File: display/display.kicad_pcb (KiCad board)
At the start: 2 copper layers, 68.4 x 20.5 mm, 48 parts, among them P1 CONN_14

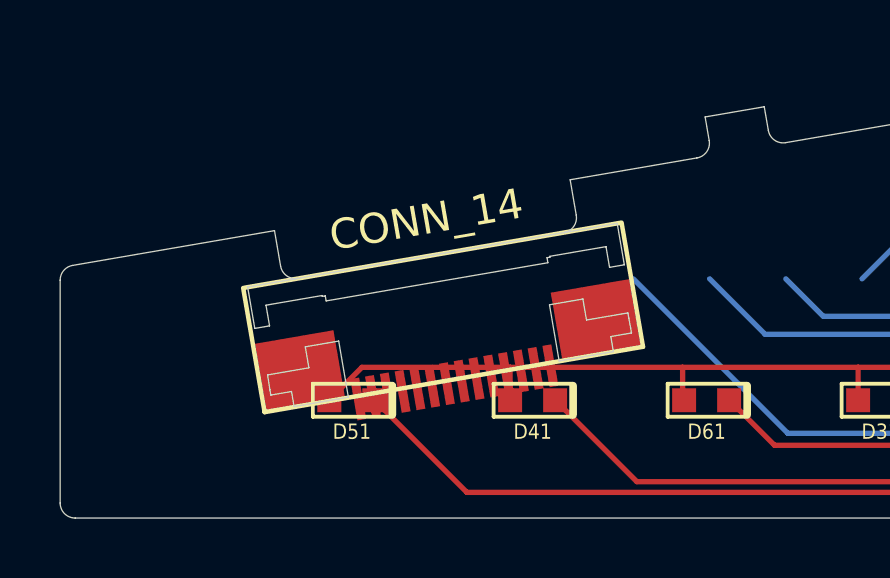
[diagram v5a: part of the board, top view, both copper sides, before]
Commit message: Remove the leftover contour lines of the connector.
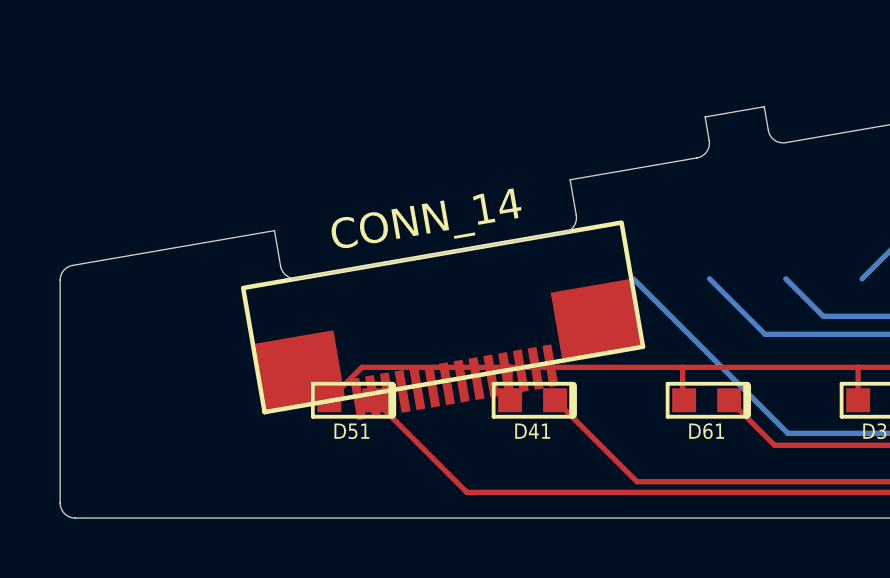
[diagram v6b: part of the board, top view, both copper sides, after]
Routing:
- net (no net): track 620.2 -> 699.0 mm, vias 29 -> 30
- net /COL7: track 78.8 -> 0.00 mm, vias 1 -> 0
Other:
- outline, holes or cut-outs redrawn

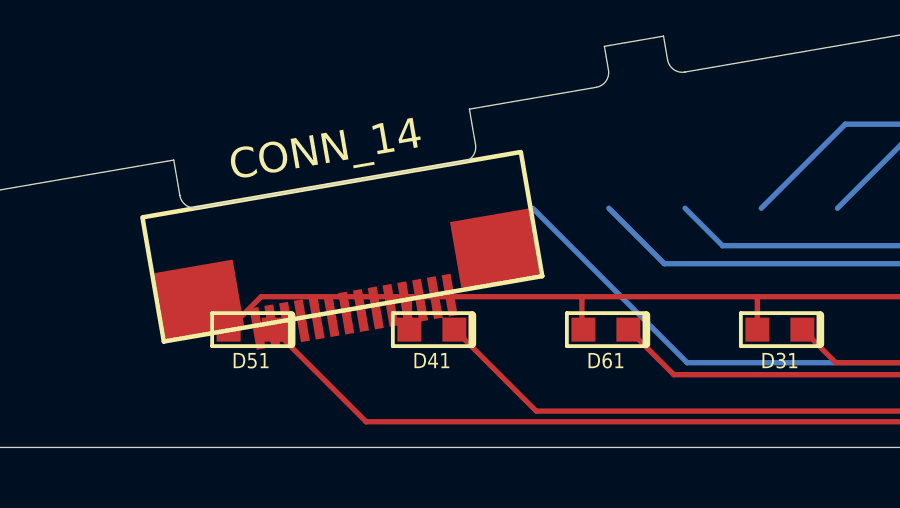
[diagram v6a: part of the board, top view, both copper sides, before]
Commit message: Remove D41 and D51 and the wires that were intersected the area of the connector.
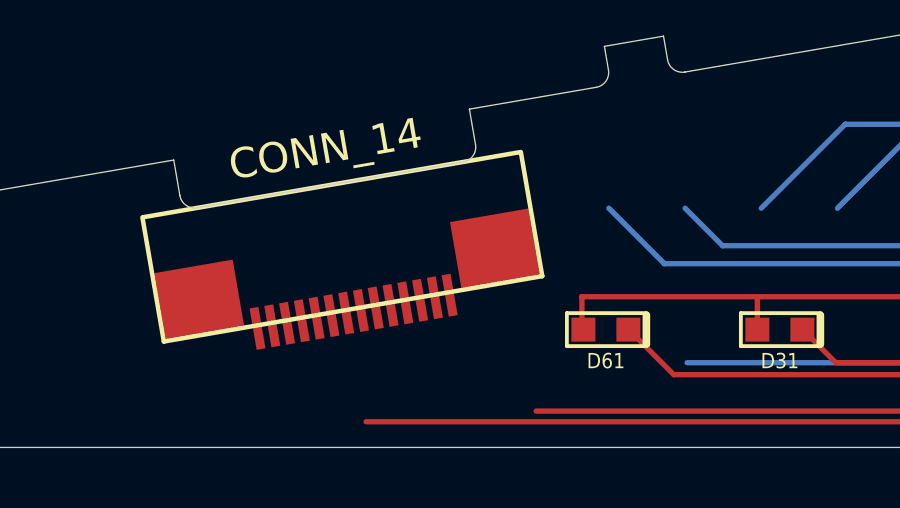
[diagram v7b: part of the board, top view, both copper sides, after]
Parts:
- removed D41, D51: LED, SM0603_Diode
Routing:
- net (no net): track 699.0 -> 670.2 mm

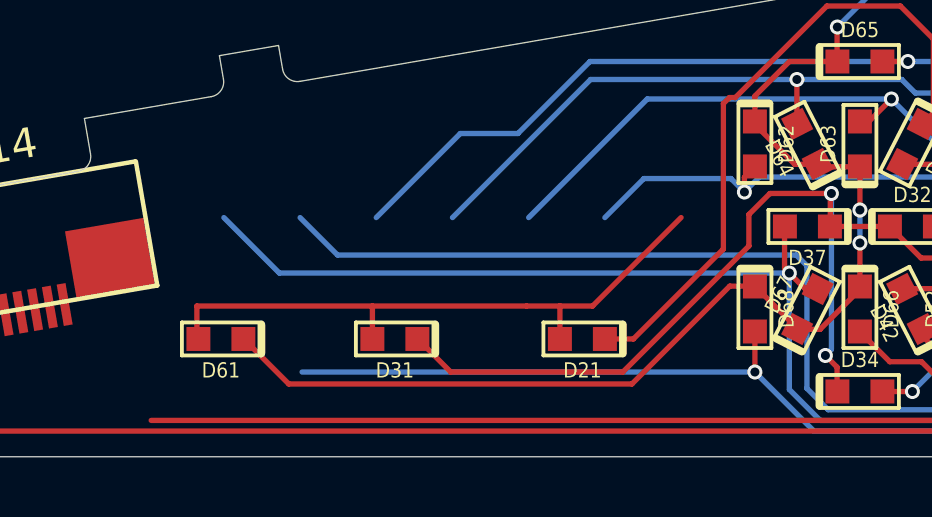
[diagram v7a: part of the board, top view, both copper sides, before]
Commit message: Update the position of D31 and D61.
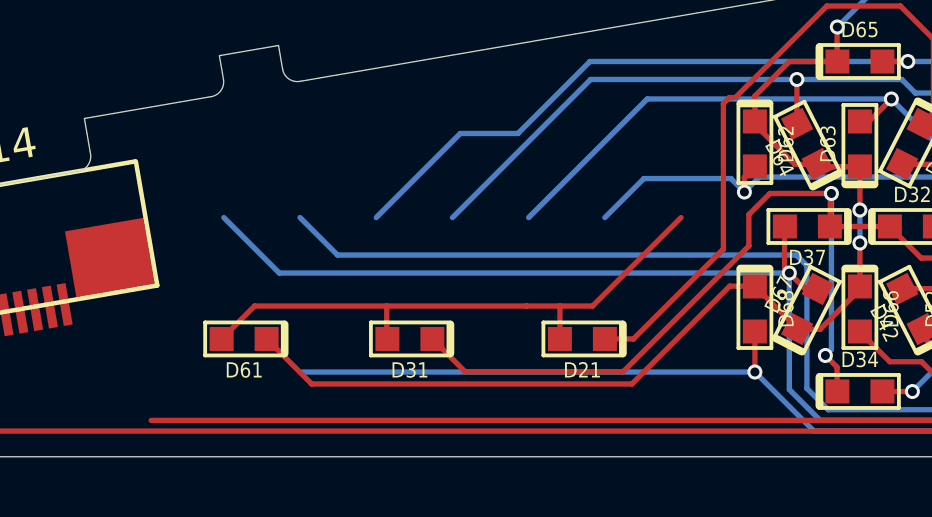
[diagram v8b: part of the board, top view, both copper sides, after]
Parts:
- moved D61 0.78 mm to (136.8, 105.8)
- moved D31 0.50 mm to (142.3, 105.8)
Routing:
- net (no net): track 670.2 -> 667.5 mm
